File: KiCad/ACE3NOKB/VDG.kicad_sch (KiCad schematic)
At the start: 40 parts, among them Q101 2N3904

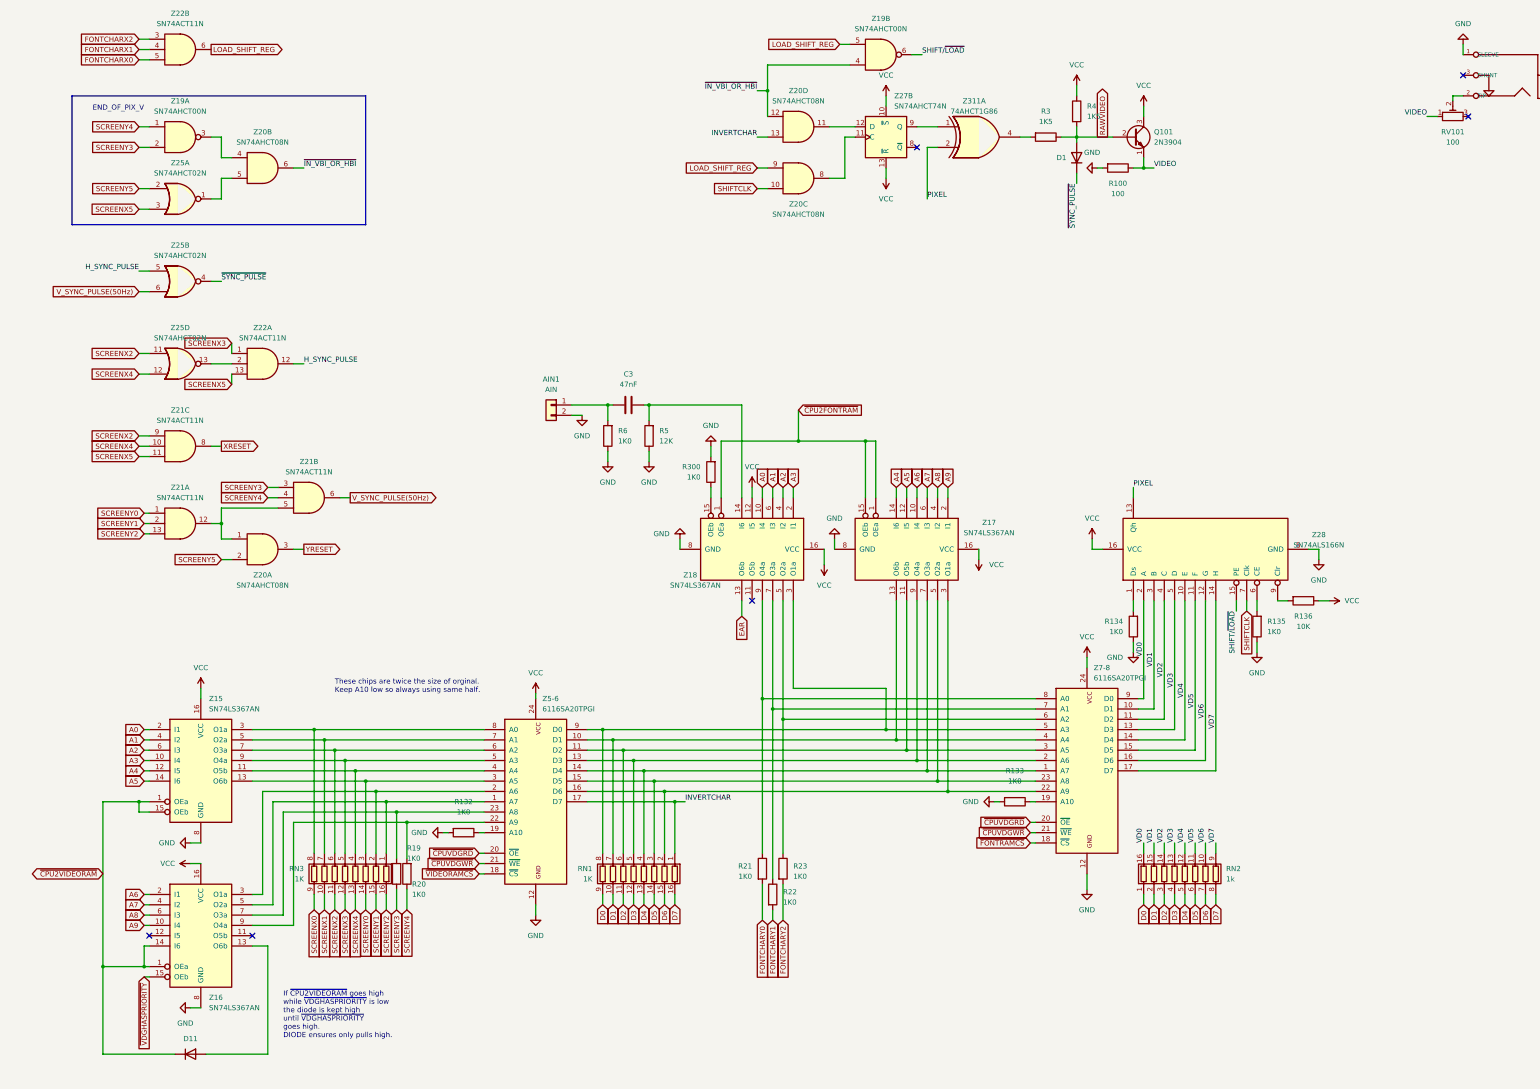
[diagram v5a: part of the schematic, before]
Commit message: Some surface mounted devices and 1G gates for space. Switch able bwteen speeds and witha Freuqency Multiplier to augment the orginal crystal.
Signed-off-by: John Bradley <flypie@rocketmail.com>
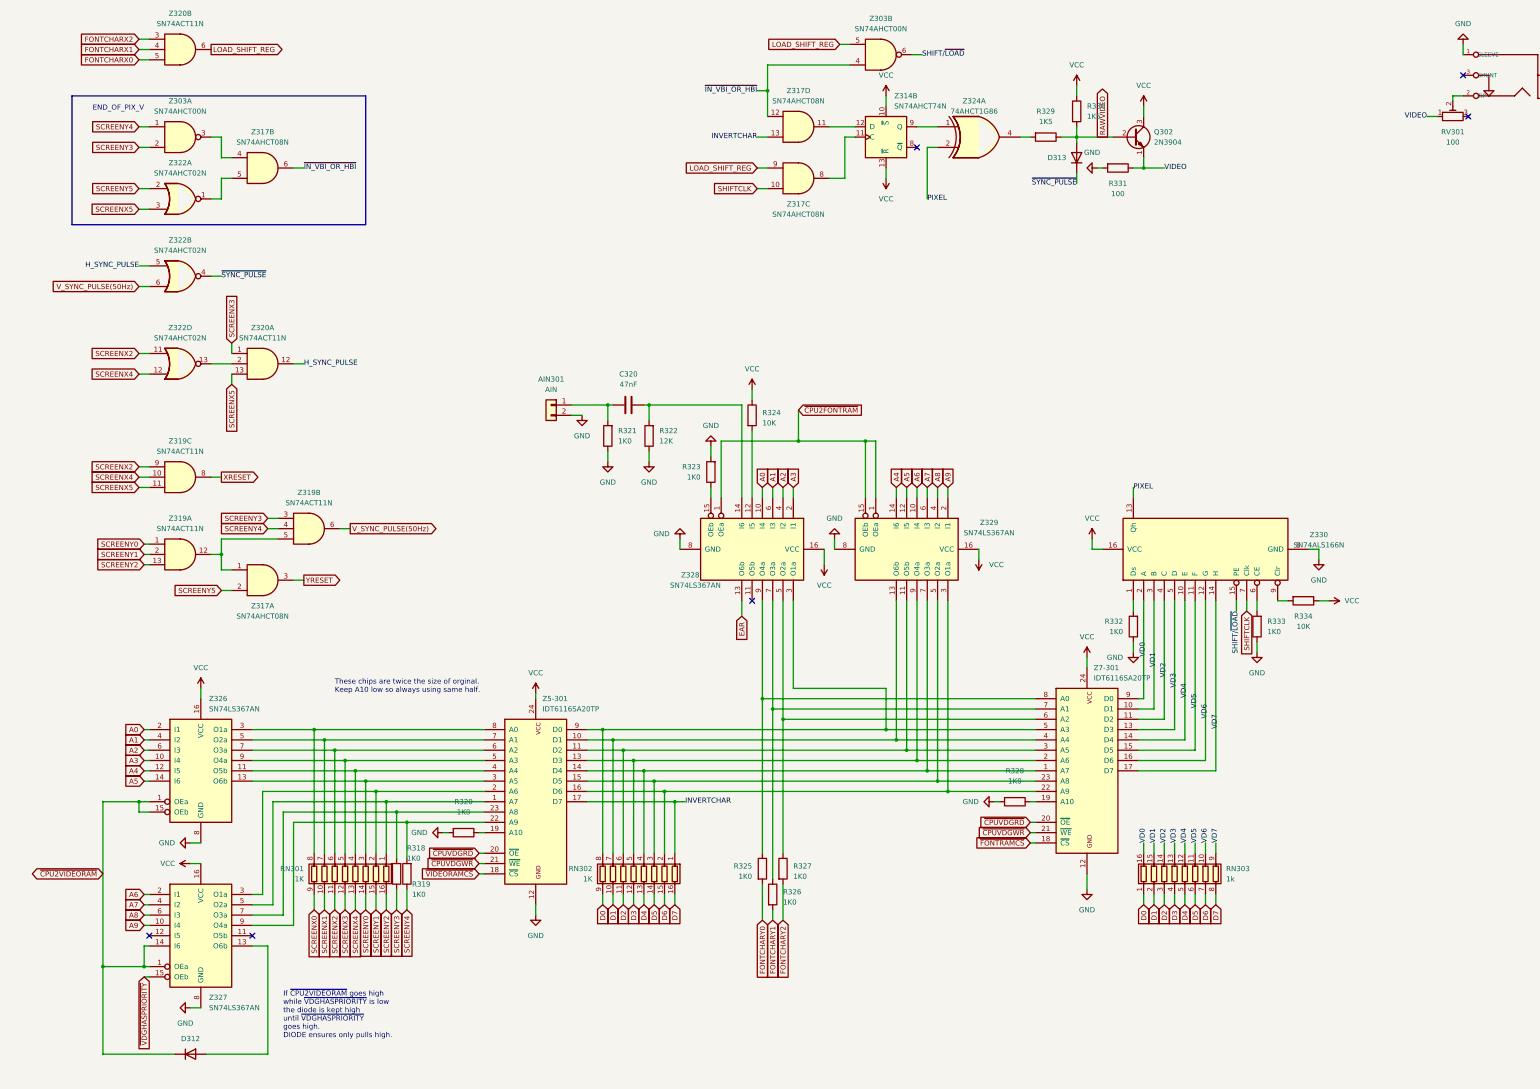
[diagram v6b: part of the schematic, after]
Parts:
- added R324: 10K, Resistor_THT:R_Axial_DIN0204_L3.6mm_D1.6mm_P1.90mm_Vertical, symbol Device:R
- Z5-301: renamed from Z5-6; value 6116SA20TPGI -> IDT6116SA20TP
- Z7-301: renamed from Z7-8; value 6116SA20TPGI -> IDT6116SA20TP
- renumbered AIN1 to AIN301, C3 to C320, COMP1 to COMP301, D11 to D312, D1 to D313, Q101 to Q302, R19 to R318, R20 to R319, R132 to R320, R6 to R321, R5 to R322, R300 to R323, R21 to R325, R22 to R326, R23 to R327, R133 to R328, R3 to R329, R4 to R330, R100 to R331, R134 to R332, R135 to R333, R136 to R334, RN3 to RN301, RN1 to RN302, RN2 to RN303, RV101 to RV301, Z19 to Z303, Z27 to Z314, Z20 to Z317, Z21 to Z319, Z22 to Z320, Z25 to Z322, Z311 to Z324, Z15 to Z326, Z16 to Z327, Z18 to Z328, Z17 to Z329, Z28 to Z330
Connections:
- net VCC: now also R324.1; no longer Z328.12 (I5)
- new net: R324.2, Z328.12 (I5)
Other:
- moved on the sheet: Z317A, Z319A, Z319B, Z319C, Z322B

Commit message: Update, with new Clock Multiplier and Wait functionality.
Signed-off-by: John Bradley <flypie@rocketmail.com>
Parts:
- removed COMP301: PJRAN1X1U03, ExtraFootprints:PJRAN1X1U01X, symbol ExtraSymbols:PJRAN1X1U03AUX
- added COMP301: PJRAN1X1U04X, ExtraFootprints:SWITCHCRAFT_PJRAN1X1U04X_CIRCULAR, symbol PJRAN1X1U04X:PJRAN1X1U04X
- Q101: renamed from Q302; footprint Package_TO_SOT_THT:TO-92_Wide -> Package_TO_SOT_THT:TO-92_Inline
- R136: renamed from R334; footprint Resistor_THT:R_Axial_DIN0204_L3.6mm_D1.6mm_P1.90mm_Vertical -> Resistor_THT:R_Axial_DIN0204_L3.6mm_D1.6mm_P2.54mm_Vertical
- R3: renamed from R329; footprint Resistor_THT:R_Axial_DIN0204_L3.6mm_D1.6mm_P1.90mm_Vertical -> Resistor_THT:R_Axial_DIN0204_L3.6mm_D1.6mm_P2.54mm_Vertical
- R317: renamed from R318; footprint Resistor_THT:R_Axial_DIN0204_L3.6mm_D1.6mm_P1.90mm_Vertical -> Resistor_THT:R_Axial_DIN0204_L3.6mm_D1.6mm_P2.54mm_Vertical
- R318: renamed from R319; footprint Resistor_THT:R_Axial_DIN0204_L3.6mm_D1.6mm_P1.90mm_Vertical -> Resistor_THT:R_Axial_DIN0204_L3.6mm_D1.6mm_P2.54mm_Vertical
- R319: renamed from R320; footprint Resistor_THT:R_Axial_DIN0204_L3.6mm_D1.6mm_P1.90mm_Vertical -> Resistor_THT:R_Axial_DIN0204_L3.6mm_D1.6mm_P2.54mm_Vertical
- R320: renamed from R321; footprint Resistor_THT:R_Axial_DIN0204_L3.6mm_D1.6mm_P1.90mm_Vertical -> Resistor_THT:R_Axial_DIN0204_L3.6mm_D1.6mm_P2.54mm_Vertical
- R321: renamed from R322; footprint Resistor_THT:R_Axial_DIN0204_L3.6mm_D1.6mm_P1.90mm_Vertical -> Resistor_THT:R_Axial_DIN0204_L3.6mm_D1.6mm_P2.54mm_Vertical
- R322: renamed from R323; footprint Resistor_THT:R_Axial_DIN0204_L3.6mm_D1.6mm_P1.90mm_Vertical -> Resistor_THT:R_Axial_DIN0204_L3.6mm_D1.6mm_P2.54mm_Vertical
- R323: renamed from R324; footprint Resistor_THT:R_Axial_DIN0204_L3.6mm_D1.6mm_P1.90mm_Vertical -> Resistor_THT:R_Axial_DIN0204_L3.6mm_D1.6mm_P2.54mm_Vertical
- R324: renamed from R325; footprint Resistor_THT:R_Axial_DIN0204_L3.6mm_D1.6mm_P1.90mm_Vertical -> Resistor_THT:R_Axial_DIN0204_L3.6mm_D1.6mm_P2.54mm_Vertical
- R325: renamed from R326; footprint Resistor_THT:R_Axial_DIN0204_L3.6mm_D1.6mm_P1.90mm_Vertical -> Resistor_THT:R_Axial_DIN0204_L3.6mm_D1.6mm_P2.54mm_Vertical
- R326: renamed from R327; footprint Resistor_THT:R_Axial_DIN0204_L3.6mm_D1.6mm_P1.90mm_Vertical -> Resistor_THT:R_Axial_DIN0204_L3.6mm_D1.6mm_P2.54mm_Vertical
- R327: renamed from R328; footprint Resistor_THT:R_Axial_DIN0204_L3.6mm_D1.6mm_P1.90mm_Vertical -> Resistor_THT:R_Axial_DIN0204_L3.6mm_D1.6mm_P2.54mm_Vertical
- R330: renamed from R331; footprint Resistor_THT:R_Axial_DIN0204_L3.6mm_D1.6mm_P1.90mm_Vertical -> Resistor_THT:R_Axial_DIN0204_L3.6mm_D1.6mm_P2.54mm_Vertical
- R331: renamed from R332; footprint Resistor_THT:R_Axial_DIN0204_L3.6mm_D1.6mm_P1.90mm_Vertical -> Resistor_THT:R_Axial_DIN0204_L3.6mm_D1.6mm_P2.54mm_Vertical
- R332: renamed from R333; footprint Resistor_THT:R_Axial_DIN0204_L3.6mm_D1.6mm_P1.90mm_Vertical -> Resistor_THT:R_Axial_DIN0204_L3.6mm_D1.6mm_P2.54mm_Vertical
- R4: renamed from R330; footprint Resistor_THT:R_Axial_DIN0204_L3.6mm_D1.6mm_P1.90mm_Vertical -> Resistor_THT:R_Axial_DIN0204_L3.6mm_D1.6mm_P2.54mm_Vertical
- Z10: renamed from Z317; symbol 74xx:74LS08 -> 74xx-FIX:74LS08
- Z19: renamed from Z303; symbol 74xx:74LS00 -> 74xx-FIX:74LS00
- Z21: renamed from Z319; symbol 74xx:74LS11 -> 74xx-FIX:74LS11
- Z22: renamed from Z320; symbol 74xx:74LS11 -> 74xx-FIX:74LS11
- Z23: renamed from Z324; symbol 74xGxx:74AHCT1G86 -> MY74xGxx:74AHCT1G86
- Z25: renamed from Z322; symbol 74xx:74LS02 -> 74xx-FIX:74LS02
- renumbered C320 to C3, D313 to D10, D312 to D11, Z326 to Z15, Z327 to Z16, Z329 to Z17, Z328 to Z18, Z314 to Z27, Z330 to Z28, Z5-301 to Z5-6, Z7-301 to Z7-8
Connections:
- net GND: now also COMP301.1
- net at RV301.2: now also COMP301.2
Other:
- note added: "If ~{CPU2VIDEORAM} goes low while ~{VDGHASPRIORITY} is low the diode is keeps it high until ~{VDGHASPRIORITY} goes high. DIODE ensures only pulls high."
- note removed: "If ~{CPU2VIDEORAM} goes high while ~{VDGHASPRIORITY} is low the diode is kept high until ~{VDGHASPRIORITY} goes high. DIODE ensures only pulls high."
- moved on the sheet: R327, RV301

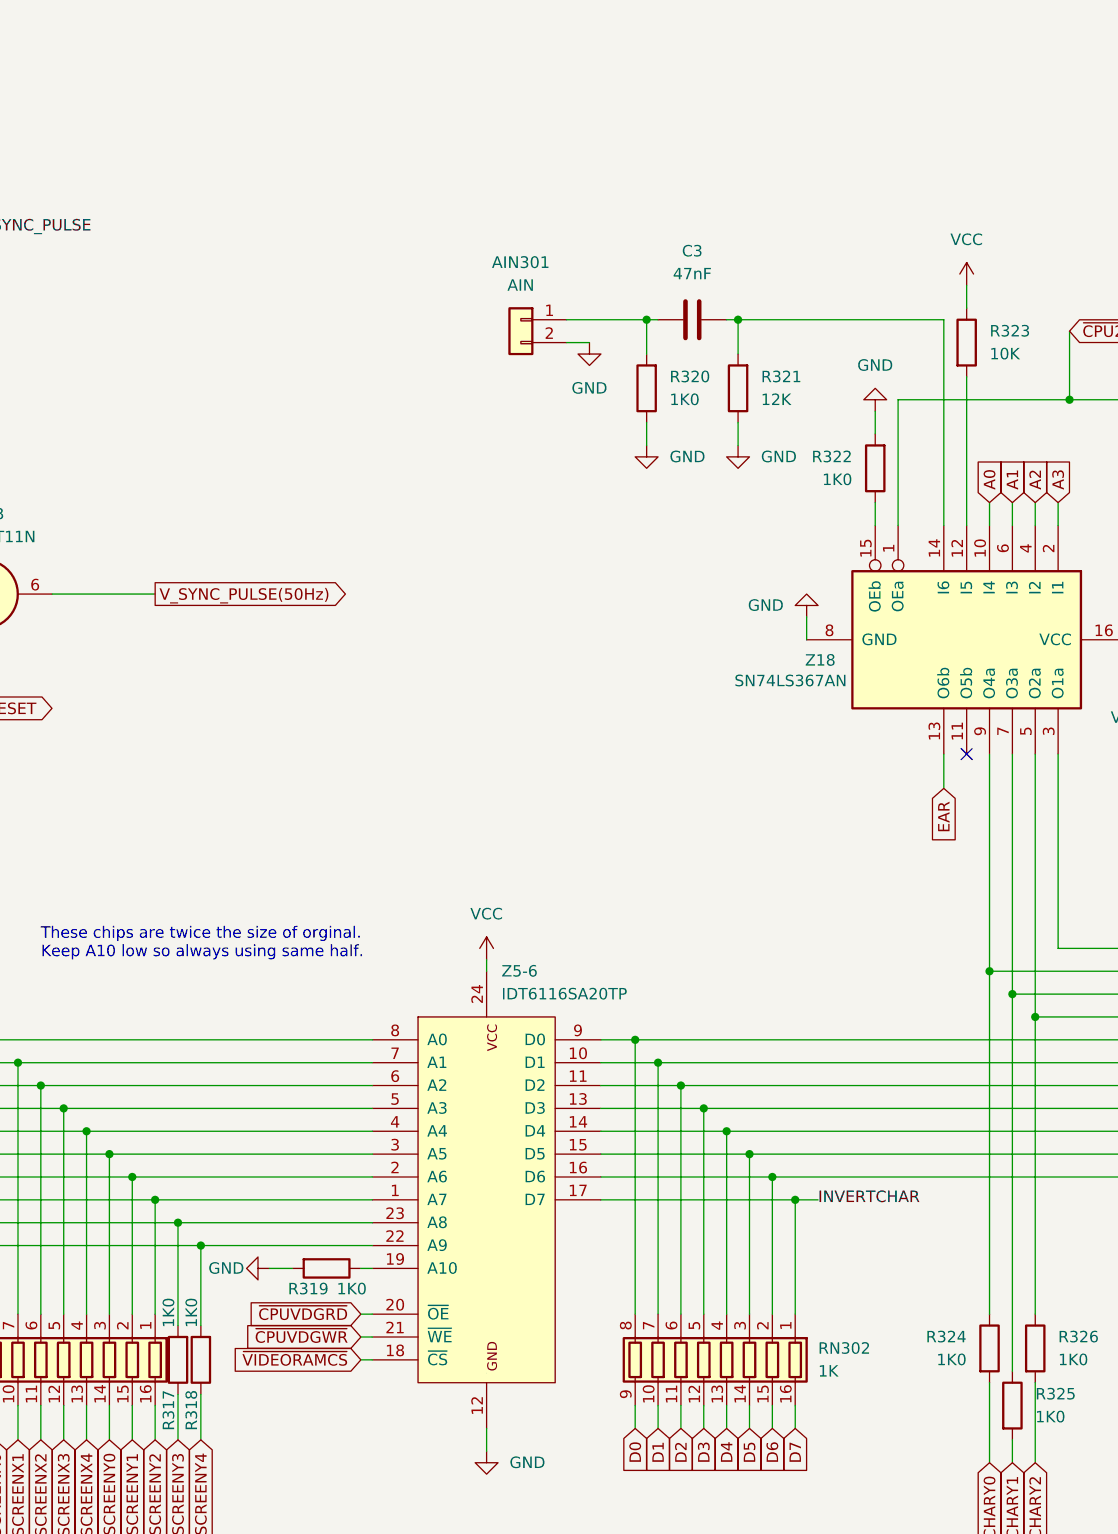
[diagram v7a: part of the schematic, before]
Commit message: Change Address decode to speed up the use of /WAIT to avoid conflicts when setting up character RAM. Rerange priority on Internal external /WAIT. Reconnect Clock to rest of circuit.
Signed-off-by: John Bradley <flypie@rocketmail.com>
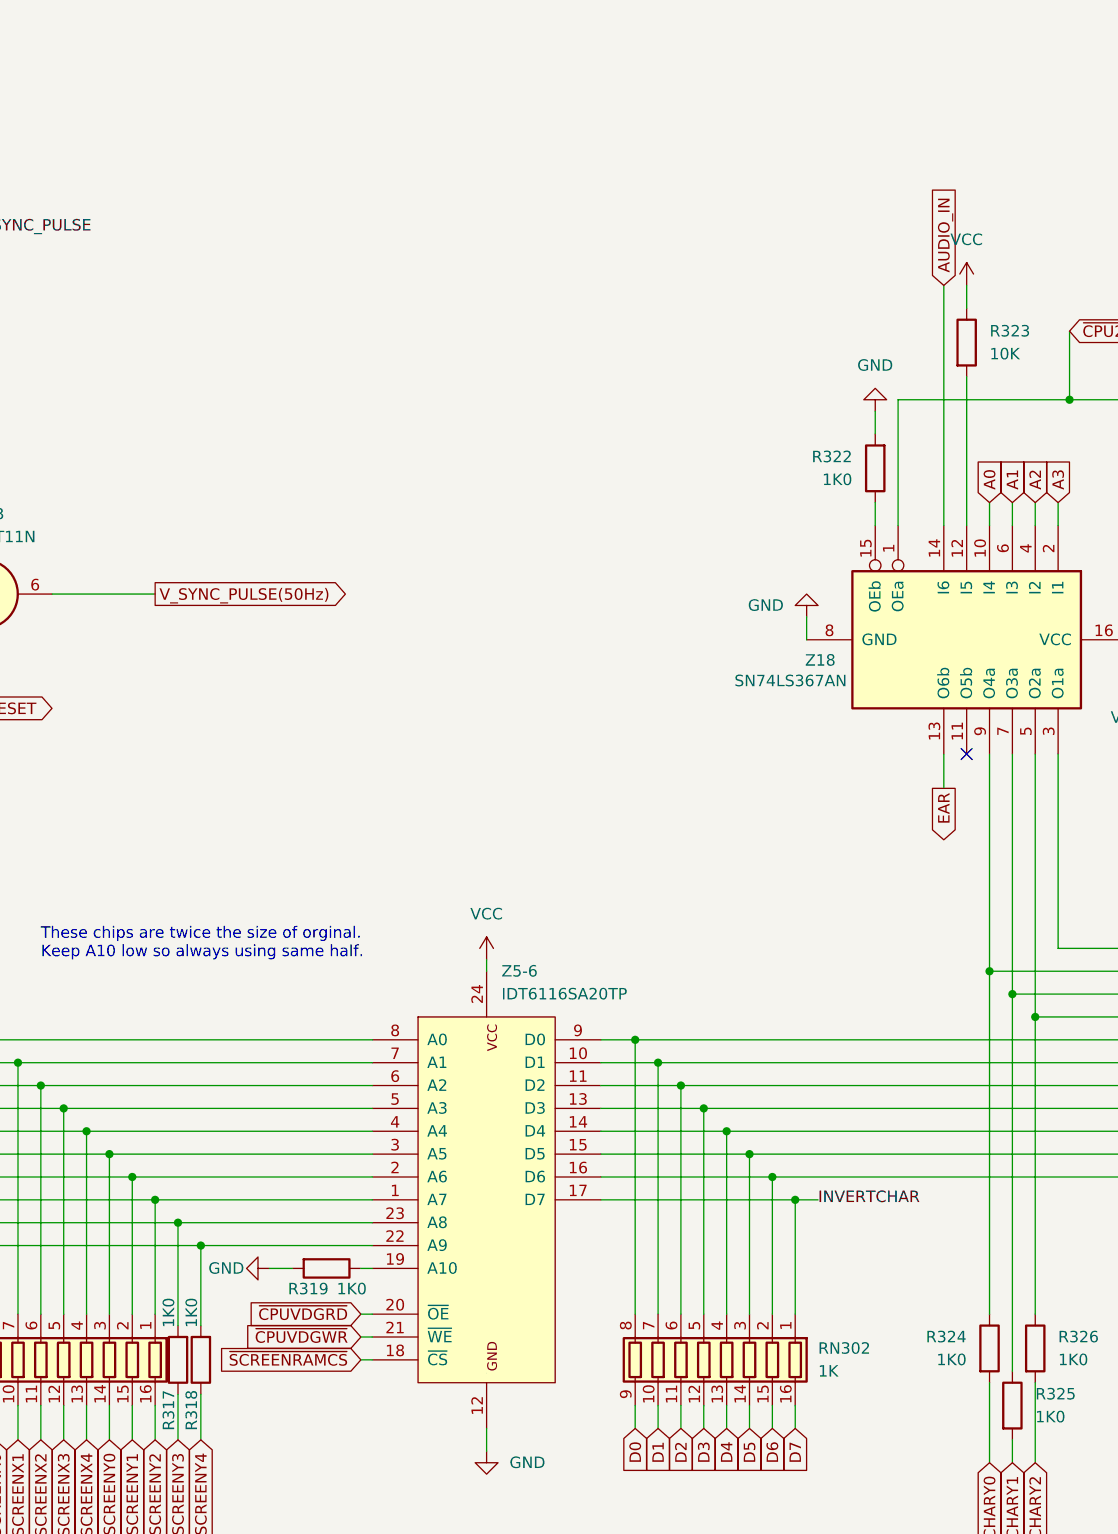
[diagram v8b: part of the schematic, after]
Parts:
- removed AIN301: AIN, Connector_PinHeader_2.54mm:PinHeader_1x02_P2.54mm_Vertical, symbol Connector_Generic:Conn_01x02
- removed C3: 47nF, Capacitor_THT:C_Disc_D5.0mm_W2.5mm_P2.50mm, symbol Device:C
- removed R320: 1K0, Resistor_THT:R_Axial_DIN0204_L3.6mm_D1.6mm_P2.54mm_Vertical, symbol Device:R
- removed R321: 12K, Resistor_THT:R_Axial_DIN0204_L3.6mm_D1.6mm_P2.54mm_Vertical, symbol Device:R
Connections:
- net AUDIO_IN: now reaches Z18.14 (I6)
- net ~{VIDEORAMCS} renamed ~{SCREENRAMCS}
